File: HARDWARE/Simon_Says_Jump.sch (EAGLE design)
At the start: 33 parts, among them J1 RJ45, J2 RJ45, J3 RJ45, J4 RJ45, J6 5V, Q1 NPN, Q2 P-Channel MOSFET, Q3 NPN, Q4 P-Channel MOSFET, Q5 NPN, Q6 P-Channel MOSFET, Q7 NPN, Q8 P-Channel MOSFET, U1 3.3V Pro Mini, U2 RFM69_BOB

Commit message: logic level converters for the range finders
They need 5V Logic on trigger and echo pins.

Also, they're gonna need power (durp), so I stole one of the GND lines in the ethernet connectors/cables to be a dedicated 5V (aka RAW) to power the range sensors.
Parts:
- added B1, B2: LOGIC, SparkFun-Boards:SPARKFUN_LOGIC_LEVEL_CONVERTER
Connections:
- new net ECHO1_5V: B2.HV_TXO_1, J1.8
- new net ECHO2_5V: B2.HV_RXI_1, J2.8
- new net ECHO3_5V: B2.HV_RXI_2, J3.8
- new net ECHO4_5V: B2.HV_TXO_2, J4.8
- new net RANGE_TRIGGER_5V: B1.HV_TXO_1, J1.7, J2.7, J3.7, J4.7
- net 3.3V: now also B1.LV, B2.LV
- net ECHO1: now also B2.LV_TXI_1; no longer J1.8
- net ECHO2: now also B2.LV_RXO_1; no longer J2.8
- net ECHO3: now also B2.LV_RXO_2; no longer J3.8
- net ECHO4: now also B2.LV_TXI_2; no longer J4.8
- net GND: now also B1.GND, B1.GND@2, B2.GND, B2.GND@2; no longer J1.1, J2.1, J3.1, J4.1
- net RANGE_TRIGGER: now also B1.LV_TXI_1, U1.PD5(T1); no longer J1.7, J2.7, J3.7, J4.7
- net RAW: now also B1.HV, B2.HV, J1.1, J2.1, J3.1, J4.1
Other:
- moved on the sheet: J1, J2, J3, J4, J7

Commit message: About to switch to 3 trampoline control
Thought I'd do a commit here, because this could be a god fork point for the SFE installed 4-trampoline setup.
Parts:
- removed B1, B2: LOGIC, SparkFun-Boards:SPARKFUN_LOGIC_LEVEL_CONVERTER
- removed S2: (no value), SparkFun:SWITCH-SPSTKIT
- removed SG1: BUZZER, SparkFun:BUZZERKIT
- added C13: 0.1uF, SparkFun:CAP0603-CAP
- added C5, C6: 10uF, SparkFun:CAP_POL1206
- added IC1: (no value), SparkFun:V_REG_LM1117SOT223
- added J10: B3, SparkFun-Connectors:CONN_03LONGPADS
- added J11: (no value), SparkFun-Connectors:CONN_06LONGPADS
- added J12, J13: (no value), SparkFun-Connectors:CONN_02PTH3
- added J14: B4, SparkFun-Connectors:CONN_03LONGPADS
- added J15: B5, SparkFun-Connectors:CONN_03LONGPADS
- added J16: B6, SparkFun-Connectors:CONN_03LONGPADS
- added J17: B7, SparkFun-Connectors:CONN_03LONGPADS
- added J8: B1, SparkFun-Connectors:CONN_03LONGPADS
- added J9: B2, SparkFun-Connectors:CONN_03LONGPADS
- added R1: 390, SparkFun:RESISTOR0603-RES
- added R10: 240, SparkFun:RESISTOR0603-RES
- added R11: 10K, SparkFun:RESISTOR0603-RES
- added R12, R13, R14, R15, R16, R17, R18: 1k, SparkFun-Resistors:1KOHM-0603-1/10W-1%
- J5: device SparkFun-Connectors:CONN_02 -> SparkFun-Connectors:CONN_02PTH3
- J7: device SparkFun-Connectors:CONN_03LOCK -> SparkFun-Connectors:CONN_03LONGPADS
- U1: value 3.3V Pro Mini -> 5V Pro Mini
- U2: value RFM69_BOB -> LOGIC; device SparkFun-Boards:RFM69_BOB -> SparkFun-Boards:SPARKFUN_LOGIC_LEVEL_CONVERTER
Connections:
- removed net BUZZER1: SG1.1, U1.PD4(XCK/T0)
- removed net BUZZER2: S2.S, U1.PD7(AIN1)
- removed net D10: U1.PB2(SS/OC1B), U2.S
- removed net D2: U1.PD2(INT0), U2.0
- removed net ECHO1_5V: B2.HV_TXO_1, J1.8
- removed net ECHO2_5V: B2.HV_RXI_1, J2.8
- removed net ECHO3_5V: B2.HV_RXI_2, J3.8
- removed net ECHO4_5V: B2.HV_TXO_2, J4.8
- removed net MISO: U1.PB4(MISO), U2.O
- removed net RANGE_TRIGGER_5V: B1.HV_TXO_1, J1.7, J2.7, J3.7, J4.7
- removed net RAW: B1.HV, B2.HV, C1.+, C2.+, C3.+, C4.+, J1.1, J2.1, J3.1, J4.1, J5.2, J7.1, Q2.S, Q4.S, Q6.S, Q8.S, R2.2, R3.2, R6.2, R8.2, U1.RAW
- new net 5V: C1.+, C2.+, C3.+, C4.+, C6.+, IC1.IN, J1.1, J12.1, J13.1, J2.1, J3.1, J4.1, J5.2, J7.1, Q2.S, Q4.S, Q6.S, Q8.S, R11.2, R2.2, R3.2, R6.2, R8.2, U1.VCC, U2.HV
- new net B1_LED: J8.2, U1.PB0(ICP)
- new net B2_LED: J9.2, U1.PB1(OC1A)
- new net B3_LED: J10.2, U1.PB2(SS/OC1B)
- new net B4_LED: J14.2
- new net B5_LED: J15.2
- new net B6_LED: J16.2
- new net B7_LED: J17.2
- new net BUTTONS: R11.1, R12.1, U1.PC7(ADC7)
- new net N$11: IC1.ADJ, R1.2, R10.1
- new net N$13: J10.1, R14.2, R15.1
- new net N$14: J14.1, R15.2, R16.1
- new net N$15: J15.1, R16.2, R17.1
- new net N$16: J16.1, R17.2, R18.1
- new net N$17: J17.1, R18.2
- new net N$6: J9.1, R13.2, R14.1
- new net SW_SER_TX_3.3V: J7.2, U2.LV_TXI_1
- net 3.3V: now also C13.1, C5.+, IC1.OUT, R10.2, U2.LV; no longer B1.LV, B2.LV, U1.VCC, U2.3.3V
- net ECHO1: now also J1.8, U1.PD2(INT0); no longer B2.LV_TXI_1, U1.PD3(INT1)
- net ECHO2: now also J2.8, U1.PD3(INT1); no longer B2.LV_RXO_1, U1.PD6(AIN0)
- net ECHO3: now also J3.8, U1.PD4(XCK/T0); no longer B2.LV_RXO_2, U1.PB1(OC1A)
- net ECHO4: now also J4.8, U1.PD5(T1); no longer B2.LV_TXI_2, U1.PB0(ICP)
- net GND: now also C13.2, C5.-, C6.-, J10.3, J11.5, J11.6, J12.2, J13.2, J14.3, J15.3, J16.3, J17.3, J8.3, J9.3, R1.1, U2.GND@2; no longer B1.GND, B1.GND@2, B2.GND, B2.GND@2, U2.G, U2.G2
- net LED1_CTRL: now also J11.1
- net LED2_CTRL: now also J11.2
- net LED3_CTRL: now also J11.3
- net LED4_CTRL: now also J11.4
- net MOSI: no longer U2.I
- net N$2: now also J8.1, R12.2, R13.1; no longer S2.P, SG1.2
- net RANGE_TRIGGER: now also J1.7, J2.7, J3.7, J4.7, U1.PD6(AIN0); no longer B1.LV_TXI_1, U1.PD5(T1)
- net SCK: no longer U2.C
- net SW_SER_TX: now also U2.HV_TXO_1; no longer J7.2
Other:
- note removed: "3.3V SYSTEM"
- note removed: "D10"
- note removed: "D11"
- note removed: "D12"
- note removed: "D13"
- note removed: "D2"
- note removed: "D3"
- note removed: "D4"
- note removed: "D5"
- note removed: "D6"
- note removed: "D7"
- note removed: "D8"
- note removed: "D9"
- note removed: "Pro Mini"
- moved on the sheet: J5, U1

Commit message: Ready for layout
Opted to keep 4 trampoline/led controls. I ended up using some of the LED control lines as also control lines to the 7-segment, because I won't need to use both of these at the same time.

The toddler trampline is the only one that uses the 7-segment, and it will only use 2 buttons, so button 5,6,7 can be used for 7-segment.

Also added in 12V barrel jack input for 7-segment.

-added ethernet connector for control cable to overhead lights. These IO will control the beefcake relay boards that live up in the rafters with the can lights.
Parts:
- added J18: (no value), SparkFun-Connectors:CONN_06LONGPADS
- added J19: 12V, SparkFun:POWER_JACKPTH_LOCK
- added J20: RJ45, SparkFun-Connectors:RJ45-8
- added J21, J22: 12V, SparkFun-Connectors:CONN_02PTH3
- J11: value (none) -> LED_CTRLS
- J12, J13: value (none) -> 5V
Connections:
- removed net B5_LED: J15.2
- removed net B6_LED: J16.2
- removed net B7_LED: J17.2
- removed net MOSI: U1.PB3(MOSI/OC2)
- removed net SCK: U1.PB5(SCK)
- new net 12V: J18.6, J19.PWR, J21.1, J22.1
- new net CLK/B6_LED: J16.2, J18.3, U1.PD6(AIN0)
- new net LAT/B5_LED: J15.2, J18.2, U1.PD5(T1)
- new net SER/B7_LED: J17.2, J18.4, U1.PD7(AIN1)
- net 5V: now also J18.5
- net B1_LED: now also U1.PB5(SCK); no longer U1.PB0(ICP)
- net B4_LED: now also U1.PB3(MOSI/OC2)
- net ECHO4: now also U1.PB0(ICP); no longer U1.PD5(T1)
- net GND: now also J18.1, J19.GND, J19.GNDBREAK, J20.3, J20.6, J20.7, J20.8, J21.2, J22.2
- net LED1_CTRL: now also J20.1
- net LED2_CTRL: now also J20.2
- net LED3_CTRL: now also J20.4
- net LED4_CTRL: now also J20.5
- net RANGE_TRIGGER: now also U1.PB4(MISO); no longer U1.PD6(AIN0)
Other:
- note added: "Large Digit Driver"

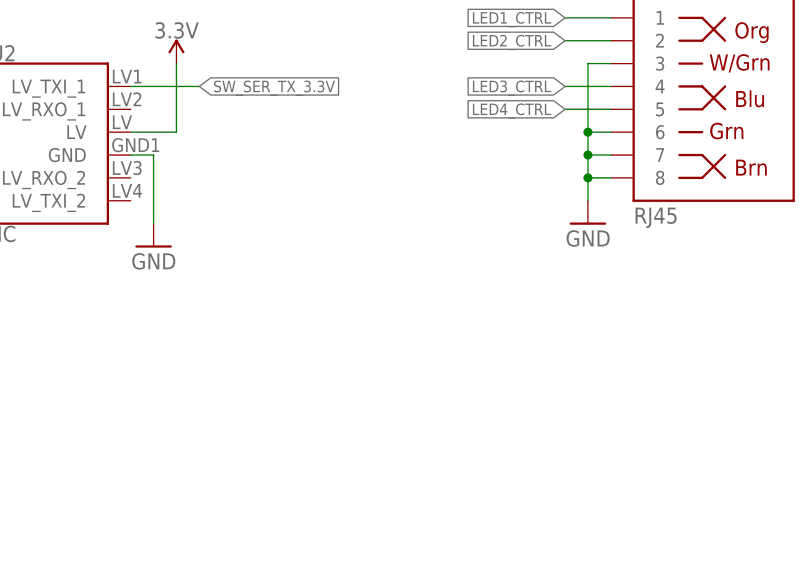
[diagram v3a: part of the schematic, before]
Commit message: Layout on main board complete
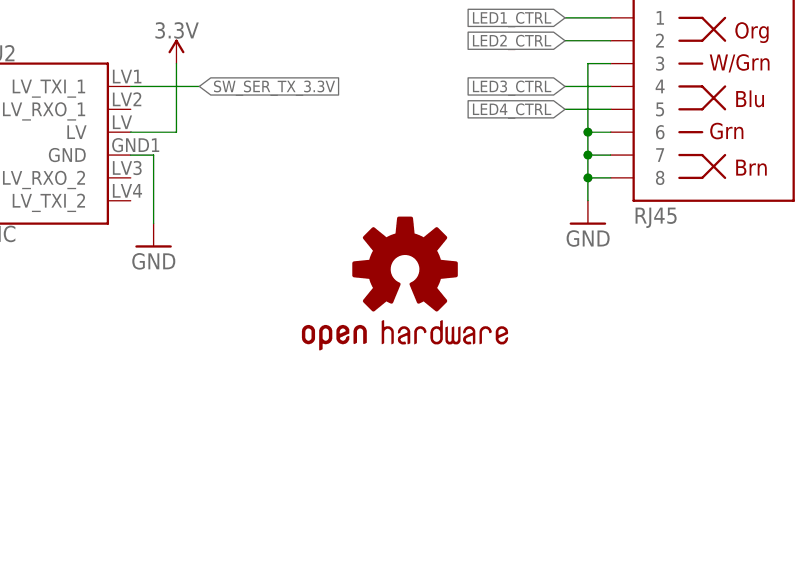
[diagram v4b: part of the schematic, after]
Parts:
- added LOGO1: OSHW-LOGOL, SparkFun-Aesthetics:OSHW-LOGOL
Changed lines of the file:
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@@
 <?xml version="1.0" encoding="utf-8"?>
 <!DOCTYPE eagle SYSTEM "eagle.dtd">
-<eagle version="7.6.0">
+<eagle version="6.5.0">
 <drawing>
 <settings>
@@
 <part name="GND25" library="SparkFun" deviceset="GND" device=""/>
 <part name="SUPPLY17" library="SparkFun-PowerSymbols" deviceset="VCC" device="" value="12V"/>
+<part name="LOGO1" library="SparkFun-Aesthetics" deviceset="OSHW-LOGO" device="L"/>
 </parts>
 <sheets>
@@
 <instance part="GND25" gate="1" x="297.18" y="33.02"/>
 <instance part="SUPPLY17" gate="G$1" x="299.72" y="60.96"/>
+<instance part="LOGO1" gate="G$1" x="195.58" y="45.72"/>
 </instances>
 <busses>
